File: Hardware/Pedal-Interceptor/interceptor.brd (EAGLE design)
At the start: 32.7 x 46.2 mm, 44 parts, among them U1 STM32-M-64-LQFP, U2 MIC5233-5.0YM5-TR, U3 MIC5233-3.3YM5-TR, U4 TJA1042HVSON, U6 MCP6002, Y1 16MHz

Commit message: Pedal fix
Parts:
- added SJ1: (no value), jumper:SJ_2
- added U5: MIC5233-5.0YM5-TR, SamacSys_Parts:SOT95P280X145-5N
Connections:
- new net N$12: SJ1.2, U$3.6
- new net N$14: SJ1.1, U5.5
- net 5V: now also SJ1.3, U5.1, U5.3; no longer U$3.6
- net GND: now also U5.2
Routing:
- net 5V: track 69.1 -> 80.9 mm
- net N$12: track 0.00 -> 3.15 mm
- net N$14: track 0.00 -> 2.22 mm
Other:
- board text added: "2.5V"
- board text added: "5V"
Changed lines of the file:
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@@
 <layers>
 <layer number="1" name="Top" color="4" fill="1" visible="yes" active="yes"/>
-<layer number="2" name="Route2" color="16" fill="1" visible="no" active="yes"/>
+<layer number="2" name="Route2" color="16" fill="1" visible="yes" active="yes"/>
 <layer number="3" name="Route3" color="17" fill="1" visible="no" active="no"/>
 <layer number="4" name="Route4" color="18" fill="1" visible="no" active="no"/>
@@
 <layer number="13" name="Route13" color="21" fill="1" visible="no" active="no"/>
 <layer number="14" name="Route14" color="22" fill="1" visible="no" active="no"/>
-<layer number="15" name="Route15" color="23" fill="1" visible="no" active="yes"/>
+<layer number="15" name="Route15" color="23" fill="1" visible="yes" active="yes"/>
 <layer number="16" name="Bottom" color="1" fill="1" visible="yes" active="yes"/>
 <layer number="17" name="Pads" color="2" fill="1" visible="yes" active="yes"/>
@@
 <hole x="16.3" y="10" drill="3"/>
 <hole x="16.3" y="43.8" drill="3"/>
+<text x="22.8" y="4.6" size="1.4224" layer="26" rot="MR270">5V</text>
+<text x="19.6" y="5" size="1.4224" layer="26" rot="MR270">2.5V</text>
 </plain>
 <attributes>
@@
 <attribute name="NAME" x="5.33" y="28.77" size="0.6096" layer="21" rot="R270"/>
 </element>
+<element name="U5" library="SamacSys_Parts" package="SOT95P280X145-5N" value="MIC5233-5.0YM5-TR" x="16" y="4" smashed="yes" rot="MR90">
+<attribute name="DESCRIPTION" value="MICROCHIP - MIC5233-5.0YM5-TR - LDO, REG, 36VIN, 0.1A, 5V, 2%, 5SOT23" x="16" y="4" size="1.778" layer="28" rot="MR90" display="off"/>
+<attribute name="HEIGHT" value="1.45mm" x="16" y="4" size="1.778" layer="28" rot="MR90" display="off"/>
+<attribute name="MANUFACTURER_NAME" value="Microchip" x="16" y="4" size="1.778" layer="28" rot="MR90" display="off"/>
+<attribute name="MANUFACTURER_PART_NUMBER" value="MIC5233-5.0YM5-TR" x="16" y="4" size="1.778" layer="28" rot="MR90" display="off"/>
+<attribute name="MOUSER_PART_NUMBER" value="998-MIC5233-5.0YM5TR" x="16" y="4" size="1.778" layer="28" rot="MR90" display="off"/>
+<attribute name="MOUSER_PRICE-STOCK" value="https://www.mouser.co.uk/ProductDetail/Microchip-Technology-Micrel/MIC5233-50YM5-TR?qs=U6T8BxXiZAWSnpCHgrMajw%3D%3D" x="16" y="4" size="1.778" layer="28" rot="MR90" display="off"/>
+<attribute name="NAME" x="16" y="7" size="1.27" layer="26" rot="MR0" align="center"/>
+</element>
+<element name="SJ1" library="jumper" library_urn="urn:adsk.eagle:library:252" package="SJ_2" package3d_urn="urn:adsk.eagle:package:15474/1" value="" x="20.3" y="6.2" smashed="yes" rot="MR180">
+<attribute name="POPULARITY" value="7" x="20.3" y="6.2" size="1.778" layer="28" rot="MR180" display="off"/>
+<attribute name="VALUE" x="20.1999" y="6.2" size="0.02" layer="28" rot="MR180"/>
+</element>
 </elements>
 <signals>
@@
 <wire x1="18.88" y1="40.42" x2="18" y2="41.3" width="0.508" layer="16"/>
 <via x="18" y="41.3" extent="1-16" drill="0.5"/>
+<contactref element="U5" pad="2"/>
+<wire x1="19.29" y1="44.02" x2="23.13" y2="41.86" width="0" layer="19" extent="16-16"/>
+<wire x1="18" y1="41.3" x2="19.29" y2="44.02" width="0" layer="19" extent="16-16"/>
+<wire x1="19.16" y1="37.12" x2="18.88" y2="39.47" width="0" layer="19" extent="1-16"/>
+<wire x1="15.31" y1="37.29" x2="17.38" y2="39.17" width="0" layer="19" extent="16-16"/>
+<wire x1="14.11" y1="37.12" x2="15.31" y2="37.29" width="0" layer="19" extent="1-16"/>
+<wire x1="13.9959" y1="35.155" x2="14.11" y2="37.12" width="0" layer="19" extent="1-1"/>
+<wire x1="18.94" y1="33.53" x2="19.16" y2="37.12" width="0" layer="19" extent="1-1"/>
+<wire x1="14.15" y1="30.99" x2="13.9959" y2="35.155" width="0" layer="19" extent="16-16"/>
+<wire x1="14.21" y1="27.68" x2="14.15" y2="30.99" width="0" layer="19" extent="16-16"/>
+<wire x1="13.94" y1="23.39" x2="14.21" y2="27.68" width="0" layer="19" extent="16-16"/>
+<wire x1="13.76" y1="21.52" x2="13.94" y2="23.39" width="0" layer="19" extent="1-16"/>
+<wire x1="12.5" y1="19.36" x2="13.76" y2="21.52" width="0" layer="19" extent="1-1"/>
+<wire x1="10.47" y1="19.565" x2="12.5" y2="19.36" width="0" layer="19" extent="1-1"/>
+<wire x1="13.4" y1="17" x2="12.5" y2="19.36" width="0" layer="19" extent="1-1"/>
+<wire x1="8.76" y1="21.52" x2="10.47" y2="19.565" width="0" layer="19" extent="1-1"/>
+<wire x1="8.13" y1="23.29" x2="8.76" y2="21.52" width="0" layer="19" extent="1-16"/>
+<wire x1="9.78" y1="25.31" x2="8.13" y2="23.29" width="0" layer="19" extent="16-16"/>
+<wire x1="6.26" y1="25.52" x2="8.13" y2="23.29" width="0" layer="19" extent="1-16"/>
+<wire x1="4.8" y1="21.8" x2="7.4" y2="20.5" width="0" layer="19" extent="1-1"/>
+<wire x1="3" y1="20.52" x2="4.8" y2="21.8" width="0" layer="19" extent="1-1"/>
+<wire x1="2.727" y1="23.853" x2="4.8" y2="21.8" width="0" layer="19" extent="1-1"/>
+<wire x1="2.73" y1="25.77" x2="2.727" y2="23.853" width="0" layer="19" extent="1-1"/>
+<wire x1="4.43" y1="28.07" x2="2.73" y2="25.77" width="0" layer="19" extent="1-1"/>
+<wire x1="2.69" y1="29.91" x2="4.43" y2="28.07" width="0" layer="19" extent="1-1"/>
+<wire x1="8.51" y1="15.69" x2="10.47" y2="19.565" width="0" layer="19" extent="1-16"/>
+<wire x1="9.782" y1="31.117" x2="14.15" y2="30.99" width="0" layer="19" extent="16-16"/>
+<wire x1="8.76" y1="33.02" x2="9.782" y2="31.117" width="0" layer="19" extent="1-16"/>
+<wire x1="10.89" y1="11.78" x2="8.51" y2="15.69" width="0" layer="19" extent="16-16"/>
+<wire x1="10.89" y1="8.78" x2="10.89" y2="11.78" width="0" layer="19" extent="1-1"/>
+<wire x1="18" y1="19.12" x2="13.76" y2="21.52" width="0" layer="19" extent="1-1"/>
+<wire x1="18.871" y1="21.341" x2="18" y2="19.12" width="0" layer="19" extent="1-1"/>
+<wire x1="22.46" y1="21" x2="18.871" y2="21.341" width="0" layer="19" extent="1-1"/>
+<wire x1="22.4" y1="23.99" x2="22.46" y2="21" width="0" layer="19" extent="1-1"/>
+<wire x1="25.06" y1="25.505" x2="22.4" y2="23.99" width="0" layer="19" extent="1-1"/>
+<wire x1="25.975" y1="26.6" x2="25.06" y2="25.505" width="0" layer="19" extent="1-16"/>
+<wire x1="25.06" y1="19.055" x2="25.975" y2="17.96" width="0" layer="19" extent="1-1"/>
+<wire x1="25.98" y1="15.8" x2="25.975" y2="17.96" width="0" layer="19" extent="1-16"/>
+<wire x1="22.16" y1="15.8" x2="25.98" y2="15.8" width="0" layer="19" extent="16-16"/>
+<wire x1="27.67" y1="11.78" x2="25.98" y2="15.8" width="0" layer="19" extent="16-16"/>
+<wire x1="27.67" y1="8.78" x2="27.67" y2="11.78" width="0" layer="19" extent="1-1"/>
+<wire x1="10.47" y1="41.86" x2="14.11" y2="37.12" width="0" layer="19" extent="1-1"/>
+<wire x1="1.37" y1="36.18" x2="2.69" y2="29.91" width="0" layer="19" extent="1-1"/>
+<wire x1="16" y1="2.75" x2="10.89" y2="8.78" width="0" layer="19" extent="16-16"/>
 </signal>
 <signal name="VCAP2">
@@
 <contactref element="U3" pad="3"/>
 <contactref element="C7" pad="1"/>
-<contactref element="U$3" pad="6"/>
 <wire x1="16.66" y1="36.17" x2="14.11" y2="36.17" width="0.6096" layer="1"/>
 <wire x1="16.66" y1="36.17" x2="17.24" y2="35.59" width="0.6096" layer="1"/>
@@
 <wire x1="32" y1="27" x2="32" y2="9" width="0.6096" layer="16"/>
 <wire x1="32" y1="9" x2="30" y2="7" width="0.6096" layer="16"/>
-<wire x1="30" y1="7" x2="23.45" y2="7" width="0.6096" layer="16"/>
-<wire x1="23.45" y1="7" x2="21.67" y2="8.78" width="0.6096" layer="16"/>
-<wire x1="21.67" y1="8.78" x2="21.67" y2="11.78" width="0.6096" layer="16"/>
+<contactref element="SJ1" pad="3"/>
+<contactref element="U5" pad="3"/>
+<contactref element="U5" pad="1"/>
+<wire x1="22.624" y1="7" x2="21.824" y2="6.2" width="0.6096" layer="16"/>
+<wire x1="30" y1="7" x2="23" y2="7" width="0.6096" layer="16"/>
+<wire x1="23" y1="7" x2="22.624" y2="7" width="0.6096" layer="16"/>
+<wire x1="21.67" y1="11.78" x2="23" y2="10.45" width="0.6096" layer="16"/>
+<wire x1="23" y1="10.45" x2="23" y2="7" width="0.6096" layer="16"/>
+<wire x1="21.824" y1="6.2" x2="21.316" y2="5.692" width="0.6096" layer="16"/>
+<wire x1="21.316" y1="5.692" x2="21.316" y2="5.22104375" width="0.6096" layer="16"/>
+<wire x1="21.316" y1="5.22104375" x2="18.84495625" y2="2.75" width="0.6096" layer="16"/>
+<wire x1="18.84495625" y1="2.75" x2="16.95" y2="2.75" width="0.6096" layer="16"/>
+<wire x1="16.7318" y1="1.97114375" x2="16.47885625" y2="1.7182" width="0.6096" layer="16"/>
+<wire x1="16.47885625" y1="1.7182" x2="15.52114375" y2="1.7182" width="0.6096" layer="16"/>
+<wire x1="15.52114375" y1="1.7182" x2="15.2682" y2="1.97114375" width="0.6096" layer="16"/>
+<wire x1="16.95" y1="2.75" x2="16.7318" y2="2.5318" width="0.6096" layer="16"/>
+<wire x1="16.7318" y1="2.5318" x2="16.7318" y2="1.97114375" width="0.6096" layer="16"/>
+<wire x1="15.2682" y1="1.97114375" x2="15.2682" y2="2.5318" width="0.6096" layer="16"/>
+<wire x1="15.2682" y1="2.5318" x2="15.05" y2="2.75" width="0.6096" layer="16"/>
 </signal>
 <signal name="CAN1_RX">
@@
 <wire x1="28" y1="23" x2="28" y2="27.19" width="0.254" layer="1"/>
 </signal>
+<signal name="N$12">
+<contactref element="SJ1" pad="2"/>
+<contactref element="U$3" pad="6"/>
+<wire x1="20.3" y1="6.2" x2="20.3" y2="7.41" width="0.6096" layer="16"/>
+<wire x1="20.3" y1="7.41" x2="21.67" y2="8.78" width="0.6096" layer="16"/>
+</signal>
+<signal name="N$14">
+<contactref element="SJ1" pad="1"/>
+<contactref element="U5" pad="5"/>
+<wire x1="16.95" y1="5.25" x2="17.9" y2="6.2" width="0.6096" layer="16"/>
+<wire x1="17.9" y1="6.2" x2="18.776" y2="6.2" width="0.6096" layer="16"/>
+</signal>
 </signals>

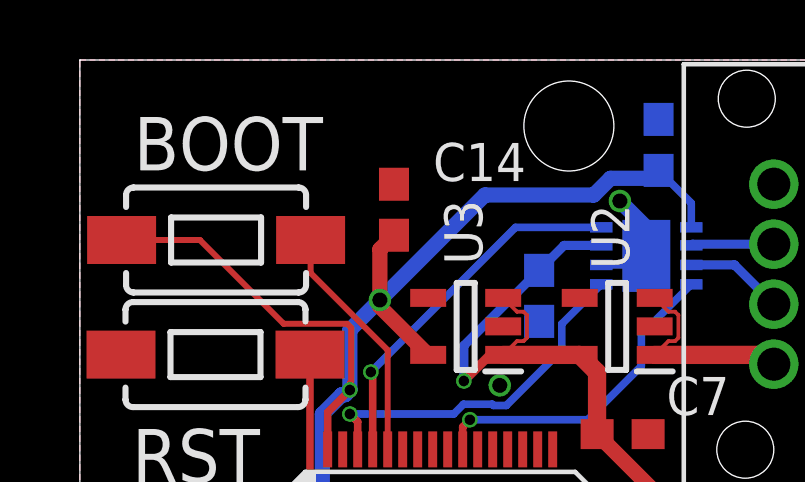
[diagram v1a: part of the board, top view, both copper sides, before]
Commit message: add pull resistors
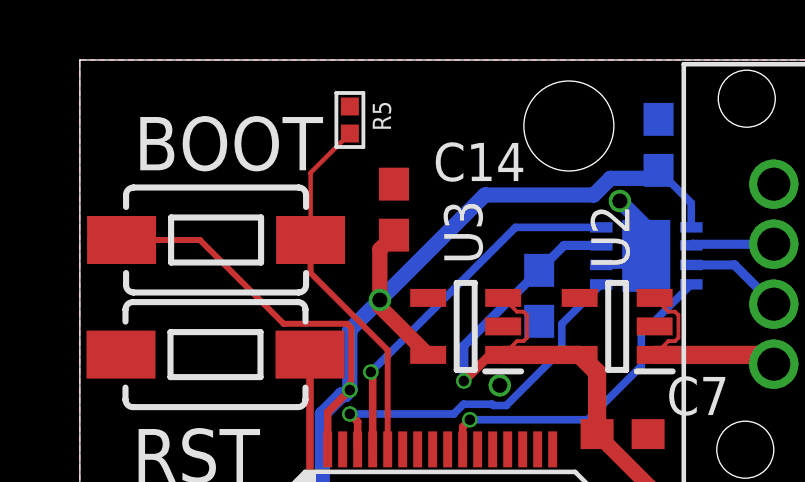
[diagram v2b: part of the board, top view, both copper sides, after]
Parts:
- added R5: (no value), comma.ai:0402-R
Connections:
- net GND: now also R5.1
- net N$7: now also R5.2
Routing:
- net N$7: track 8.04 -> 12.1 mm
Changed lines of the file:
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@@
 <attribute name="VALUE" x="20.1999" y="6.2" size="0.02" layer="28" rot="MR180"/>
+</element>
+<element name="R5" library="comma.ai" package="0402-R" value="" x="9" y="44" smashed="yes" rot="R270">
+<attribute name="NAME" x="9.762" y="44.635" size="0.6096" layer="25" rot="R270"/>
 </element>
 </elements>
@@
 <via x="18" y="41.3" extent="1-16" drill="0.5"/>
 <contactref element="U5" pad="2"/>
+<contactref element="R5" pad="1"/>
 <wire x1="19.29" y1="44.02" x2="23.13" y2="41.86" width="0" layer="19" extent="16-16"/>
 <wire x1="18" y1="41.3" x2="19.29" y2="44.02" width="0" layer="19" extent="16-16"/>
@@
 <wire x1="1.37" y1="36.18" x2="2.69" y2="29.91" width="0" layer="19" extent="1-1"/>
 <wire x1="16" y1="2.75" x2="10.89" y2="8.78" width="0" layer="19" extent="16-16"/>
+<wire x1="9" y1="44.45" x2="10.89" y2="8.78" width="0" layer="19" extent="1-1"/>
 </signal>
 <signal name="VCAP2">
@@
 <wire x1="7.69" y1="40" x2="7.69" y2="38.9" width="0.2" layer="1"/>
 <wire x1="10.26" y1="36.33" x2="10.26" y2="33.02" width="0.2" layer="1"/>
+<contactref element="R5" pad="2"/>
+<wire x1="7.69" y1="40" x2="7.69" y2="42.24" width="0.1524" layer="1"/>
+<wire x1="7.69" y1="42.24" x2="9" y2="43.55" width="0.1524" layer="1"/>
 </signal>
 <signal name="N$11">

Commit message: new boards
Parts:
- added R6: 10k, comma.ai:0402-R
- R5: value (none) -> 10k
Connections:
- net 3V3: now also R6.1
- net N$10: now also R6.2
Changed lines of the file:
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@@
 <attribute name="VALUE" x="20.1999" y="6.2" size="0.02" layer="28" rot="MR180"/>
 </element>
-<element name="R5" library="comma.ai" package="0402-R" value="" x="9" y="44" smashed="yes" rot="R270">
+<element name="R5" library="comma.ai" package="0402-R" value="10k" x="9" y="44" smashed="yes" rot="R270">
 <attribute name="NAME" x="9.762" y="44.635" size="0.6096" layer="25" rot="R270"/>
+</element>
+<element name="R6" library="comma.ai" package="0402-R" value="10k" x="1" y="-2" smashed="yes">
+<attribute name="NAME" x="0.365" y="-1.238" size="0.6096" layer="25"/>
 </element>
 </elements>
@@
 <wire x1="17.68685" y1="42.056" x2="19.026" y2="42.056" width="0.508" layer="16"/>
 <wire x1="13.5" y1="41.5" x2="17.13085" y2="41.5" width="0.508" layer="16"/>
+<contactref element="R6" pad="1"/>
+<wire x1="0.55" y1="-2" x2="9" y2="20.3" width="0" layer="19" extent="1-1"/>
 </signal>
 <signal name="N$1">
@@
 <wire x1="6.9652125" y1="28.116" x2="7.67" y2="28.8207875" width="0.254" layer="1"/>
 <wire x1="7.67" y1="28.8207875" x2="7.67" y2="36.18" width="0.254" layer="1"/>
+<contactref element="R6" pad="2"/>
+<wire x1="1.45" y1="-2" x2="6.26" y2="28.02" width="0" layer="19" extent="1-1"/>
 </signal>
 <signal name="N$7">

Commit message: Pedal v2
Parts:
- added C15: 100nF, comma.ai:0603-C
- added IC1: LM358D, comma.ai:SO08
- moved R6 35.6 mm to (6.80, 33.1), turned to 90 degrees
- moved LED1 4.40 mm to (14.5, 13.2), turned to 0 degrees
- moved R13 3.98 mm to (14.5, 18.9)
- moved C2 2.20 mm to (19.1, 20.2)
- moved C8 1.35 mm to (19.0, 22.2)
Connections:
- new net N$13: IC1.1, IC1.2, R23.2
- new net N$15: IC1.6, IC1.7, R24.2
- net 5V: now also C15.1, IC1.8
- net ACCEL1: now also IC1.3; no longer R23.2
- net ACCEL2: now also IC1.5; no longer R24.2
- net GND: now also C15.2, IC1.4
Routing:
- net 3V3: track 84.6 -> 99.2 mm
- net 5V: track 80.9 -> 92.4 mm, vias 2 -> 3
- net N$15: track 0.00 -> 7.16 mm, vias 0 -> 1
- net N$13: track 0.00 -> 7.04 mm, vias 0 -> 1
- net ACCEL1: track 3.77 -> 8.90 mm
- net LEDG: track 6.32 -> 2.25 mm
- net N$26: track 2.14 -> 4.26 mm
- net ACCEL2: track 6.15 -> 7.76 mm
- net VCAP1: track 2.83 -> 3.98 mm
- net N$10: track 9.10 -> 10.2 mm
